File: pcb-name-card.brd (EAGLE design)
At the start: 84 x 53 mm, 8 parts, among them U1 3V, U2 3V

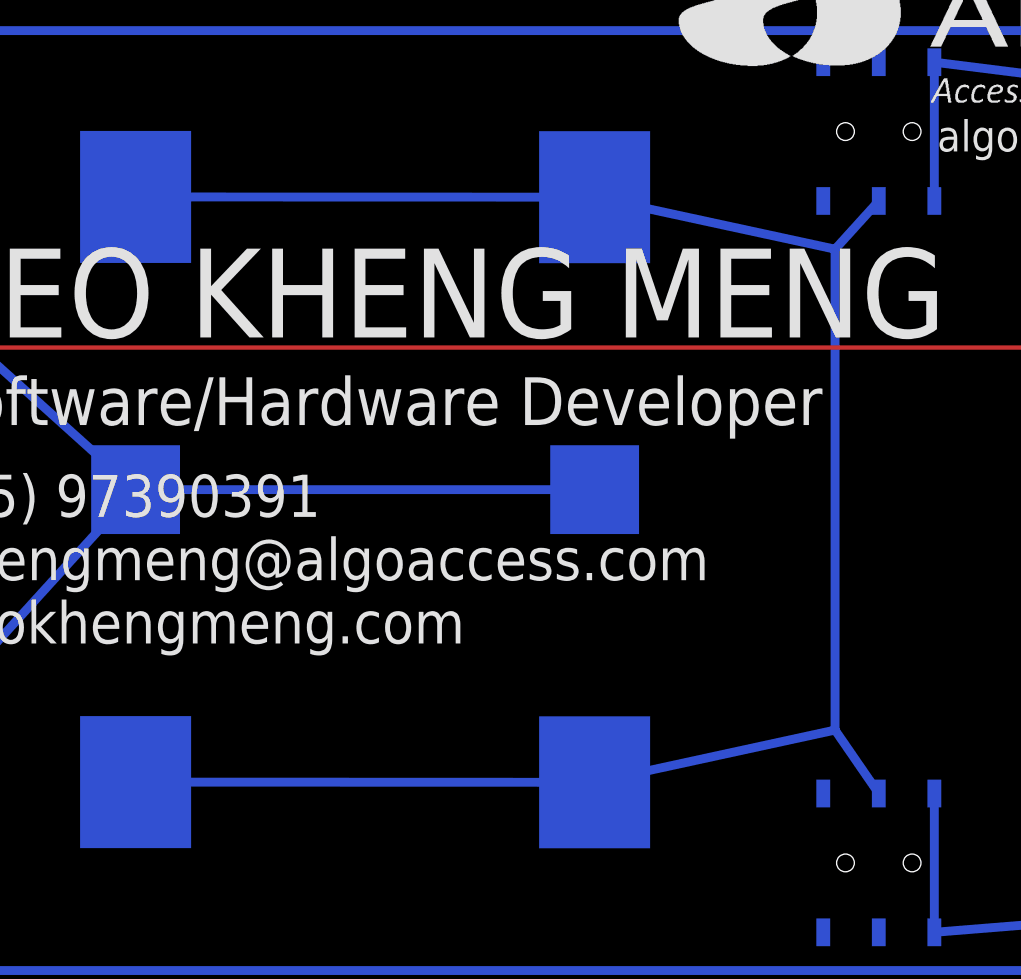
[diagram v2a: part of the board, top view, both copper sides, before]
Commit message: battery position
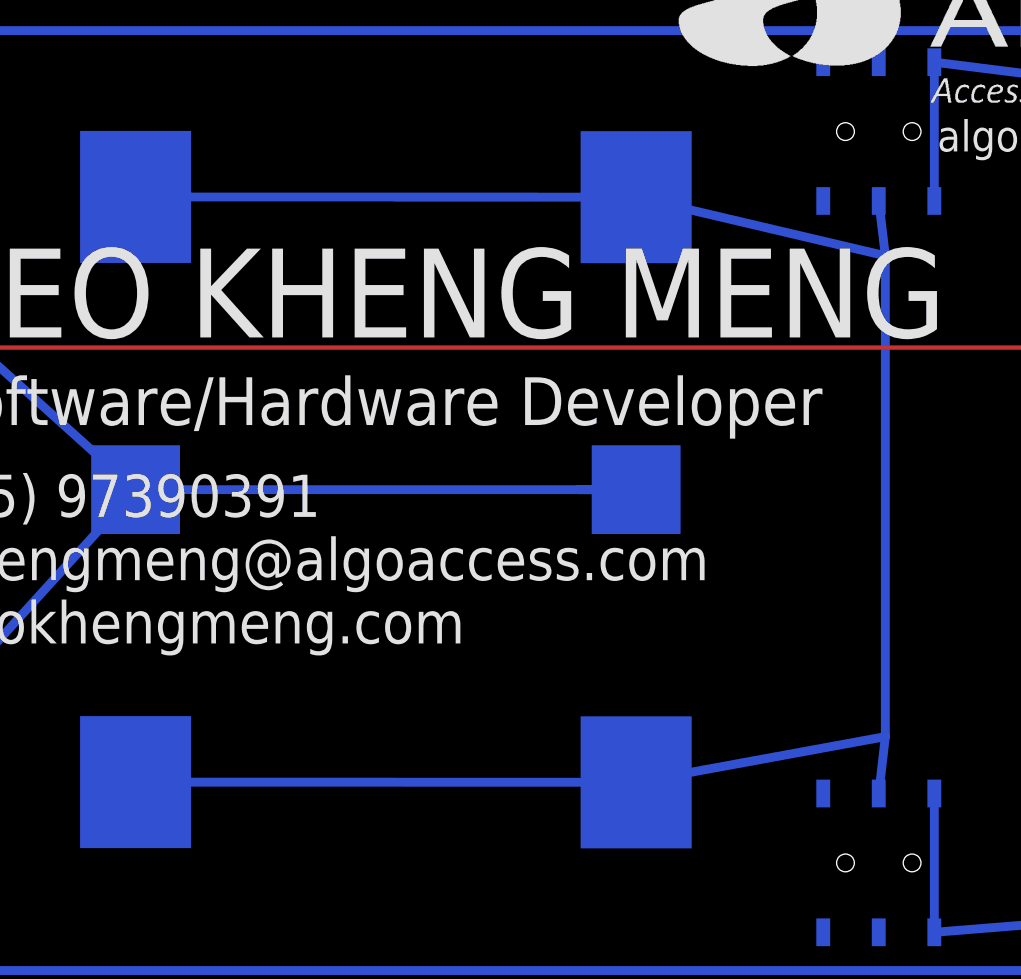
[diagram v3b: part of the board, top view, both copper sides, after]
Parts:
- moved U2 1.90 mm to (33.9, 27.0)
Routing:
- net N$7: track 242.4 -> 246.2 mm
- net N$9: track 93.0 -> 96.2 mm
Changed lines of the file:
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@@
 <grid distance="1" unitdist="mm" unit="mm" style="lines" multiple="1" display="yes" altdistance="0.1" altunitdist="mm" altunit="mm"/>
 <layers>
-<layer number="1" name="Top" color="4" fill="1" visible="yes" active="yes"/>
+<layer number="1" name="Top" color="4" fill="1" visible="no" active="yes"/>
 <layer number="2" name="Route2" color="1" fill="3" visible="no" active="no"/>
 <layer number="3" name="Route3" color="4" fill="3" visible="no" active="no"/>
@@
 <layer number="19" name="Unrouted" color="6" fill="1" visible="yes" active="yes"/>
 <layer number="20" name="Dimension" color="15" fill="1" visible="yes" active="yes"/>
-<layer number="21" name="tPlace" color="7" fill="1" visible="yes" active="yes"/>
+<layer number="21" name="tPlace" color="7" fill="1" visible="no" active="yes"/>
 <layer number="22" name="bPlace" color="7" fill="1" visible="yes" active="yes"/>
 <layer number="23" name="tOrigins" color="15" fill="1" visible="yes" active="yes"/>
@@
 <layer number="27" name="tValues" color="7" fill="1" visible="yes" active="yes"/>
 <layer number="28" name="bValues" color="7" fill="1" visible="yes" active="yes"/>
-<layer number="29" name="tStop" color="7" fill="3" visible="yes" active="yes"/>
-<layer number="30" name="bStop" color="7" fill="6" visible="yes" active="yes"/>
+<layer number="29" name="tStop" color="7" fill="3" visible="no" active="yes"/>
+<layer number="30" name="bStop" color="7" fill="6" visible="no" active="yes"/>
 <layer number="31" name="tCream" color="7" fill="4" visible="yes" active="yes"/>
 <layer number="32" name="bCream" color="7" fill="5" visible="yes" active="yes"/>
@@
 <text x="49.771078125" y="39.7722" size="1.016" layer="22" font="vector" rot="MR270">Caution: Look away from LEDs
 before toggling the switches</text>
-<text x="27.5" y="39.06" size="1.016" layer="22" font="vector" rot="MR0">CR2025/CR2016</text>
-<text x="23.21" y="19.06" size="0.8128" layer="22" font="vector" rot="MR0">Rev 3</text>
+<text x="28.5" y="38.06" size="1.016" layer="22" font="vector" rot="MR0">CR2025/CR2016</text>
+<text x="24.21" y="19.06" size="0.8128" layer="22" font="vector" rot="MR0">Rev 3</text>
 <text x="47.671403125" y="42.473115625" size="1.4224" layer="21" font="vector">algoaccess.com</text>
 <rectangle x1="55.9391" y1="44.3959" x2="56.0915" y2="44.4213" layer="21"/>
@@
 </class>
 </classes>
-<designrules name="SeeedStudio_2layer_DRU_no_angle_20140221">
+<designrules name="Elecrow_2-layer_eagle_rule">
 <description language="de">&lt;b&gt;EAGLE Design Rules&lt;/b&gt;
 &lt;p&gt;
@@
 necessary adjustments and save your customized
 design rules under a new name.</description>
-<description language="zh">&lt;b&gt;Seeed Studio EAGLE Design Rules&lt;/b&gt;
+<description language="zh">&lt;b&gt;Elecrow EAGLE Design Rules&lt;/b&gt;
 </description>
 <param name="layerSetup" value="(1*16)"/>
-<param name="mtCopper" value="0.035mm 0.0175mm 0.035mm 0.035mm 0.035mm 0.035mm 0.035mm 0.035mm 0.035mm 0.035mm 0.035mm 0.035mm 0.035mm 0.035mm 0.0175mm 0.035mm"/>
-<param name="mtIsolate" value="1.5mm 1.1mm 0.2mm 0.15mm 0.2mm 0.15mm 0.2mm 0.15mm 0.2mm 0.15mm 0.2mm 0.15mm 0.2mm 0.15mm 0.2mm"/>
+<param name="mtCopper" value="0.035mm 0.035mm 0.035mm 0.035mm 0.035mm 0.035mm 0.035mm 0.035mm 0.035mm 0.035mm 0.035mm 0.035mm 0.035mm 0.035mm 0.035mm 0.035mm"/>
+<param name="mtIsolate" value="1.5mm 0.15mm 0.2mm 0.15mm 0.2mm 0.15mm 0.2mm 0.15mm 0.2mm 0.15mm 0.2mm 0.15mm 0.2mm 0.15mm 0.2mm"/>
 <param name="mdWireWire" value="6mil"/>
 <param name="mdWirePad" value="6mil"/>
@@
 <attribute name="COLOR" value="yellow" x="80.82315" y="32.81365" size="1.778" layer="28" rot="MR180" display="off"/>
 </element>
-<element name="U2" library="cr2032-large-side" package="CR2032-SMD" value="3V" x="32" y="27" smashed="yes" rot="MR90"/>
+<element name="U2" library="cr2032-large-side" package="CR2032-SMD" value="3V" x="33.9" y="27" smashed="yes" rot="MR90"/>
 <element name="SW1" library="Seeed-OPL-Switch" package="SW6-2.54-SMD-7.0X3.5X1.5MM" value="" x="45" y="43.380309375" smashed="yes" rot="MR90">
 <attribute name="MPN" value="MS-22C01" x="45" y="43.380309375" size="1.778" layer="28" rot="MR90" display="off"/>
@@
 <contactref element="LED2" pad="C"/>
 <contactref element="LED1" pad="C"/>
-<wire x1="11" y1="27" x2="32" y2="27" width="0.4064" layer="16"/>
-<wire x1="31.241221875" y1="27" x2="32" y2="27" width="0.4064" layer="16"/>
+<wire x1="11" y1="27" x2="33.9" y2="27" width="0.4064" layer="16"/>
+<wire x1="31.241221875" y1="27" x2="33.9" y2="27" width="0.4064" layer="16"/>
 <wire x1="80.938" y1="18.2834" x2="71" y2="5" width="0.4064" layer="16"/>
 <wire x1="71" y1="5" x2="4" y2="5" width="0.4064" layer="16"/>
@@
 <contactref element="U2" pad="+$2"/>
 <contactref element="SW1" pad="COM1"/>
-<wire x1="11" y1="40.39" x2="32" y2="40.38" width="0.4064" layer="16"/>
-<wire x1="11" y1="13.62" x2="32" y2="13.61" width="0.4064" layer="16"/>
-<wire x1="32" y1="40.38" x2="43" y2="38" width="0.4064" layer="16"/>
-<wire x1="43" y1="38" x2="43" y2="16" width="0.4064" layer="16"/>
-<wire x1="43" y1="16" x2="32" y2="13.61" width="0.4064" layer="16"/>
-<wire x1="45" y1="13.0979125" x2="43" y2="16" width="0.4064" layer="16"/>
-<wire x1="45" y1="40.205309375" x2="43" y2="38" width="0.4064" layer="16"/>
+<wire x1="11" y1="40.39" x2="33.9" y2="40.38" width="0.4064" layer="16"/>
+<wire x1="11" y1="13.62" x2="33.9" y2="13.61" width="0.4064" layer="16"/>
+<wire x1="33.9" y1="40.38" x2="45.3" y2="37.7" width="0.4064" layer="16"/>
+<wire x1="45.3" y1="37.7" x2="45.3" y2="15.7" width="0.4064" layer="16"/>
+<wire x1="45.3" y1="15.7" x2="33.9" y2="13.61" width="0.4064" layer="16"/>
+<wire x1="45" y1="13.0979125" x2="45.3" y2="15.7" width="0.4064" layer="16"/>
+<wire x1="45" y1="40.205309375" x2="45.3" y2="37.7" width="0.4064" layer="16"/>
 </signal>
 <signal name="N$3">
